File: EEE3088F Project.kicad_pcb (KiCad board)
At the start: 2 copper layers, 60 x 82 mm, 84 parts, among them J1 Conn_02x16_Odd_Even, J2 Battery IN JST, M1BulkC1 10uF, M1Control1 DRV8837, M2BulkC1 10uF, M2Control1 DRV8837, M3BulkC1 10uF, M3Control1 DRV8837, M4BulkC1 10uF, M4Control1 DRV8837, Q2 AO3400A

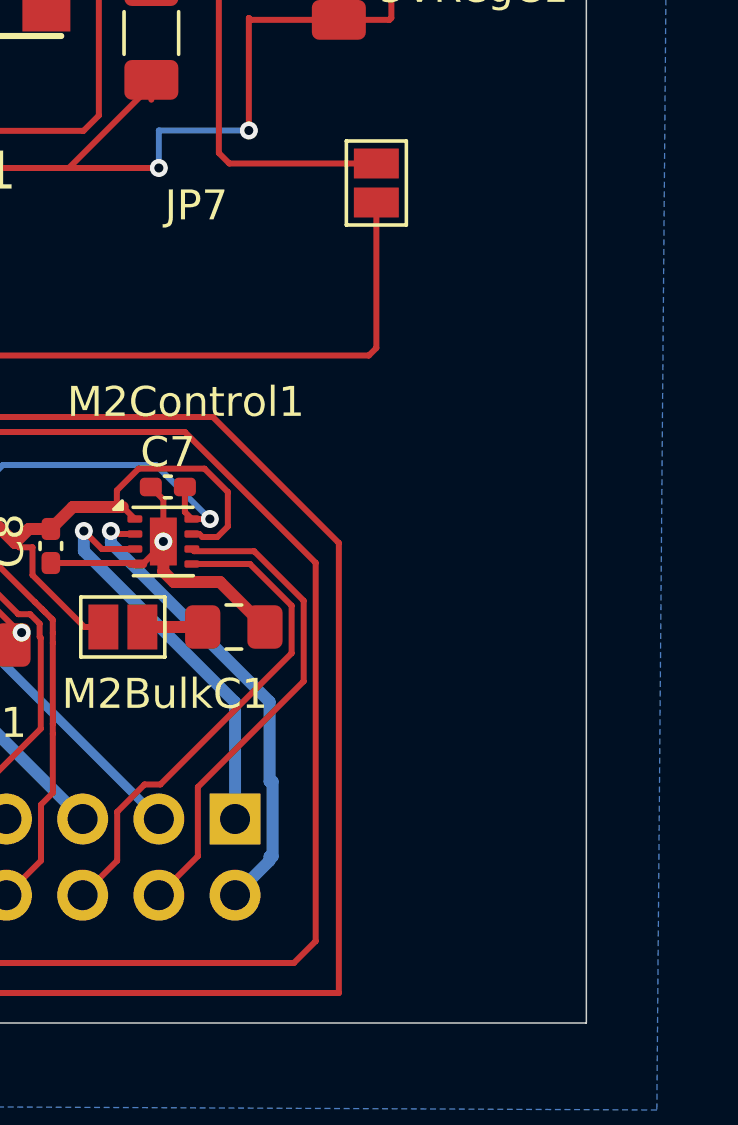
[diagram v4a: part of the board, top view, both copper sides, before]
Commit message: Minor labelling fixes. Generated gerber files
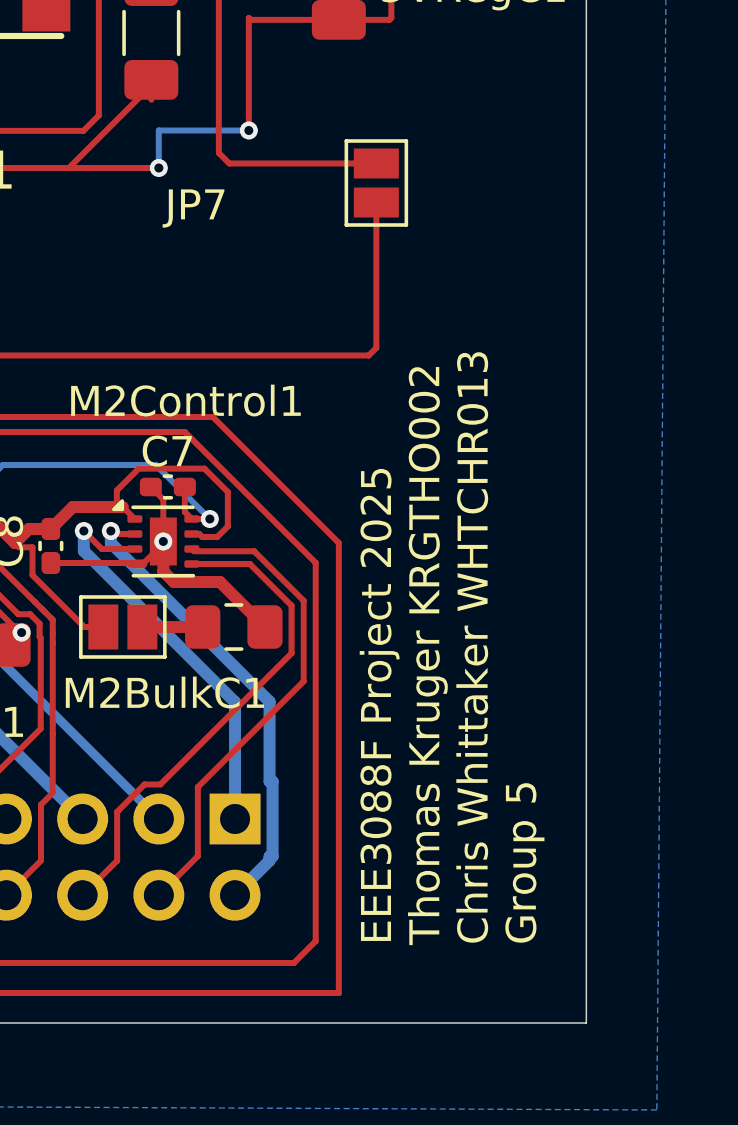
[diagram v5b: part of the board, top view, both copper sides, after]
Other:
- board text added: "EEE3088F Project 2025 Thomas Kruger KRGTHO002 Chris Whittaker WHTCHR013 Group 5"
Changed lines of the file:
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@@
 		(layer "Edge.Cuts")
+	)
+	(gr_text "EEE3088F Project 2025\nThomas Kruger KRGTHO002\nChris Whittaker WHTCHR013\nGroup 5\n\n"
+		(at 208.8 123.4 90)
+		(layer "F.SilkS")
+		(effects
+			(font
+				(size 1 1)
+				(thickness 0.1)
+			)
+			(justify left bottom)
+		)
 	)
 	(segment
